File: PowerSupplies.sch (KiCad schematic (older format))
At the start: 12 parts, among them U2 LM2937EM-5.0, U3 LM2937EM-5.0

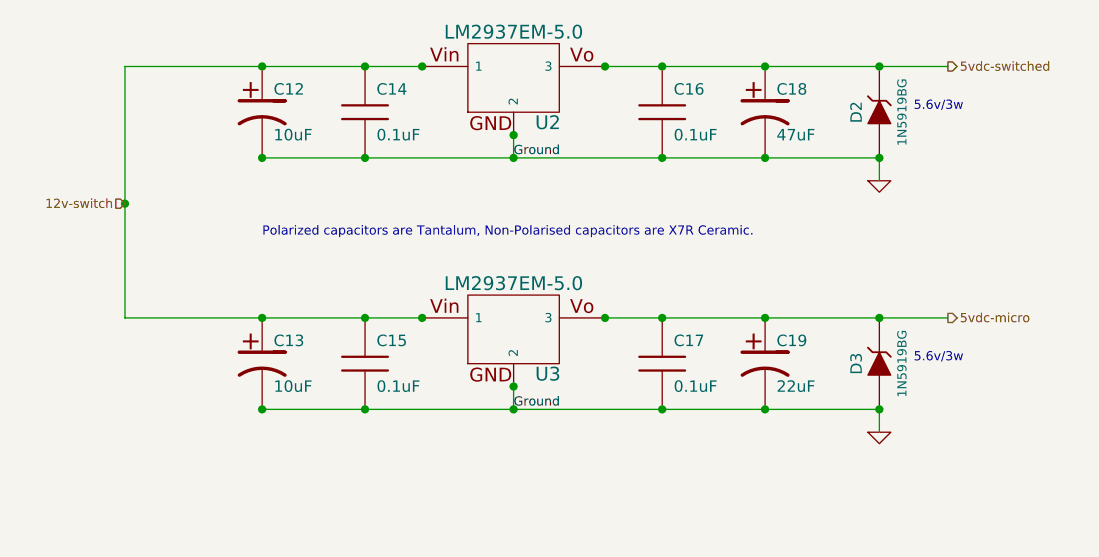
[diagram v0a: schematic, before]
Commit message: Updated Schematics, PDF, BOM for 4cyl Sequential Injection
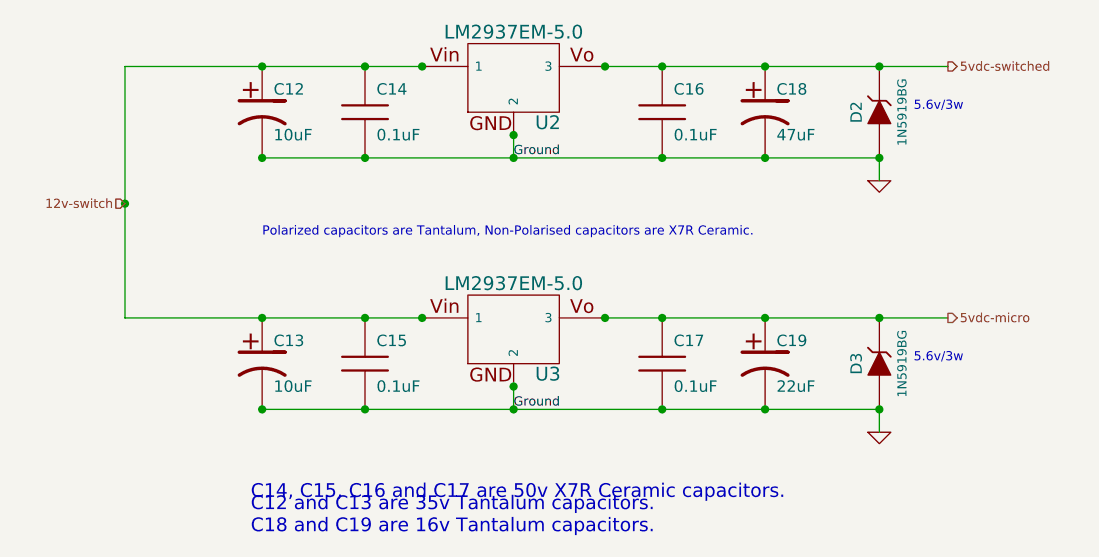
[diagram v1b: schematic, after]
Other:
- note added: "C12 and C13 are 35v Tantalum capacitors.\nC18 and C19 are 16v Tantalum capacitors."
- note added: "C14, C15, C16 and C17 are 50v X7R Ceramic capacitors."
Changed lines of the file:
@@
-EESchema Schematic File Version 2  date Tue 24 Jan 2012 02:18:15 PM EST
+EESchema Schematic File Version 2  date Tue 24 Jan 2012 11:15:10 PM EST
 LIBS:power
 LIBS:device
@@
 EELAYER END
 $Descr A4 11700 8267
-Sheet 5 7
+Sheet 7 7
 Title "Jaguar PCB for FreeEMS"
-Date "24 jan 2012"
+Date "25 jan 2012"
 Rev "A.1"
 Comp "diyefi.org"
@@
 Comment4 ""
 $EndDescr
+Text Notes 2300 4150 0    60   ~ 0
+C14, C15, C16 and C17 are 50v X7R Ceramic capacitors.
+Text Notes 2300 4300 0    60   ~ 0
+C12 and C13 are 35v Tantalum capacitors.\nC18 and C19 are 16v Tantalum capacitors.
 Connection ~ 1750 2850
 Wire Wire Line
